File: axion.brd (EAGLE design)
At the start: 100 x 80.5 mm, 148 parts, among them IC1 3.3V, IC2 5V, Q2 12.288Mhz, U10 MIC2039, U11 WM8731, U2 Intel Edison, U4 FT232RLSSOP, U5 PCA9306D, U6 74HC4050, U7 TPA2005D1DGN, X2 ZX62R-AB-5P, X3 ST-005-G, X4 ZX62R-B-5P

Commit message: Anyway, wired everything
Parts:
- removed C14, C15: 0.1u, resistor:C1608
- removed U5: PCA9306D, NXP_By_element14_Batch_1:SOIC127P600X175-8N
- added Q1, Q3: 200mA/50V, SparkFun-DiscreteSemi:SOT23-3
- added R38: 4.7k, resistor:R0603
- C24: device resistor:C0805 -> resistor:C1608
- JP26: value HDC1000 module -> HDC1000
- R1, R10, R11, R12, R13, R14, R15, R16, R17, R18, R19, R2, R20, R21, R22, R23, R24, R3, R31, R32, R34, R37, R4, R5, R6, R7, R8, R9: device resistor:M1206 -> resistor:R0603
- R25: value 200k -> 4.7k; device resistor:0309V -> resistor:R0603
- R27, R35, R40, R41, R42, R43, R44: device resistor:R1206 -> resistor:R0603
- R30, R36: value 820 -> 4.7k; device resistor:M1206 -> resistor:R0603
- moved R36 99.8 mm to (70.3, 38.5), turned to 90 degrees
- moved R30 94.3 mm to (65.3, 42.6), turned to 270 degrees
- moved JP26 52.1 mm to (82.8, 52.3), turned to 180 degrees
- moved C19 42.4 mm to (75.7, 77.4), turned to 90 degrees
- moved X2 34.5 mm to (98.0, 60.9)
- moved C16 33.5 mm to (92.8, 65.8)
- moved X4 29.5 mm to (97.8, 71.1)
- moved C2 23.5 mm to (73.8, 61.9), turned to 180 degrees
- moved R33 22.1 mm to (50.5, 47.7), turned to 90 degrees
- moved C1 21.5 mm to (30.7, 40.6)
- moved U1 21.2 mm to (32.7, 33.7)
- moved R25 20.2 mm to (50.1, 43.6), turned to 270 degrees
- moved C7 18.8 mm to (73.0, 58.9)
- moved R32 17.5 mm to (51.9, 54.8), turned to 90 degrees
- moved U3 17.4 mm to (67.6, 29.3)
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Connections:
- removed net 1V8I2S_RTX: U8.7
- removed net 3V3SCK: U11.24
- removed net 5VCLK: U3.26
- removed net N$10: C14.1, R25.2, U5.7, U5.8
- net +1V8: now also Q1.1, Q3.1, R25.1, R30.1; no longer C15.2, R30.2, R36.2, U5.2
- net +3V3: now also R36.1, R38.1; no longer R25.1
- net 1V8I2S_RXD: now also U8.7
- net 1V8SCL: now also Q1.2, R25.2; no longer R30.1, U5.3
- net 1V8SDA: now also Q3.2, R30.2; no longer R36.1, U5.4
- net 3V3SCL: now also Q1.3, R38.2, U11.24, U3.26; no longer U5.6
- net 3V3SDA: now also Q3.3, R36.2; no longer U5.5
- net DGND: no longer C14.2, C15.1, U5.1
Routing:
- net DGND: track 561.0 -> 338.9 mm, vias 4 -> 19
- net GND: track 234.9 -> 71.2 mm, vias 3 -> 4
- net N$10: track 60.7 -> 0.00 mm
- net N$39: track 46.3 -> 105.5 mm
- net 3V3SCL: track 91.1 -> 124.9 mm, vias 1 -> 5
- net USB_ID: track 79.2 -> 46.0 mm, vias 0 -> 2
- net AGND: track 168.6 -> 200.2 mm, vias 1 -> 7
- net +1V8: track 155.4 -> 128.4 mm, vias 6 -> 8
- net 1V8PWMLED: track 18.2 -> 44.9 mm, vias 3 -> 1
- net USB_DP: track 74.4 -> 51.2 mm
- net 1P0: track 31.8 -> 11.9 mm
- net 1P1: track 28.6 -> 9.12 mm
- net N$8: track 0.00 -> 19.4 mm
- net N$49: track 0.00 -> 19.4 mm
- net 1P10: track 14.5 -> 33.4 mm, vias 0 -> 2
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
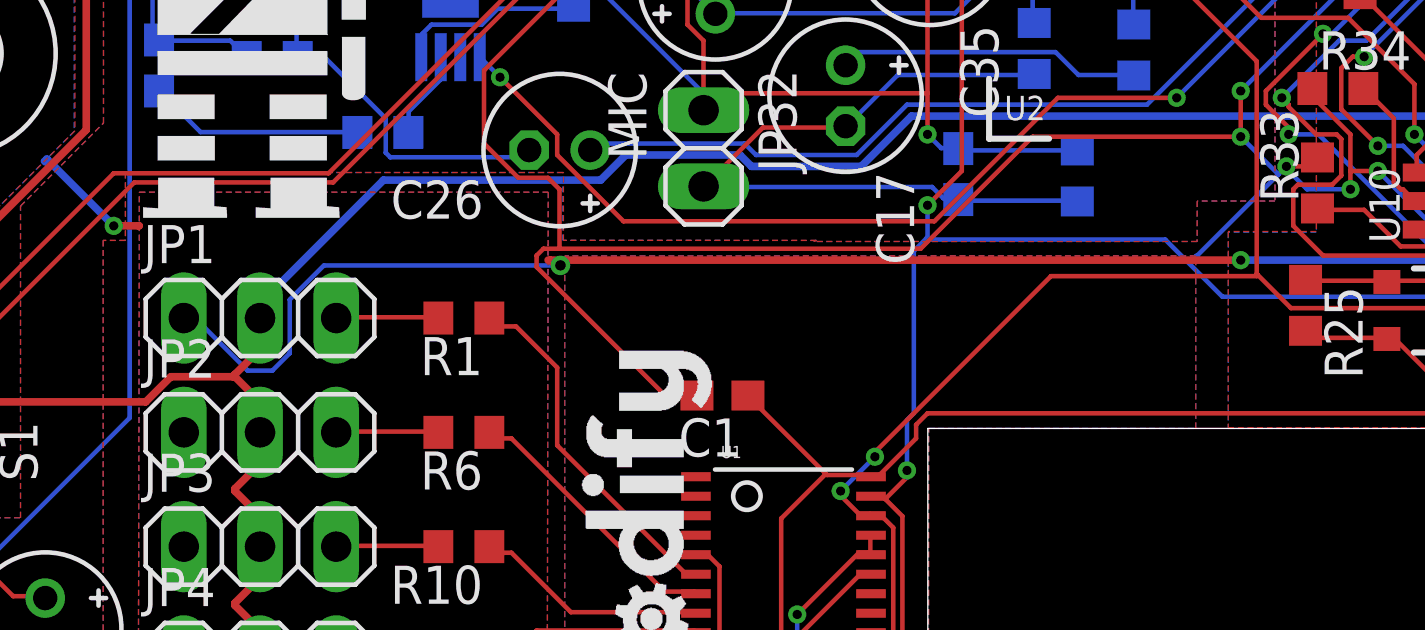
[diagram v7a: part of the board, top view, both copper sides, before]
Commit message: Fix all 'Width' DRC errors
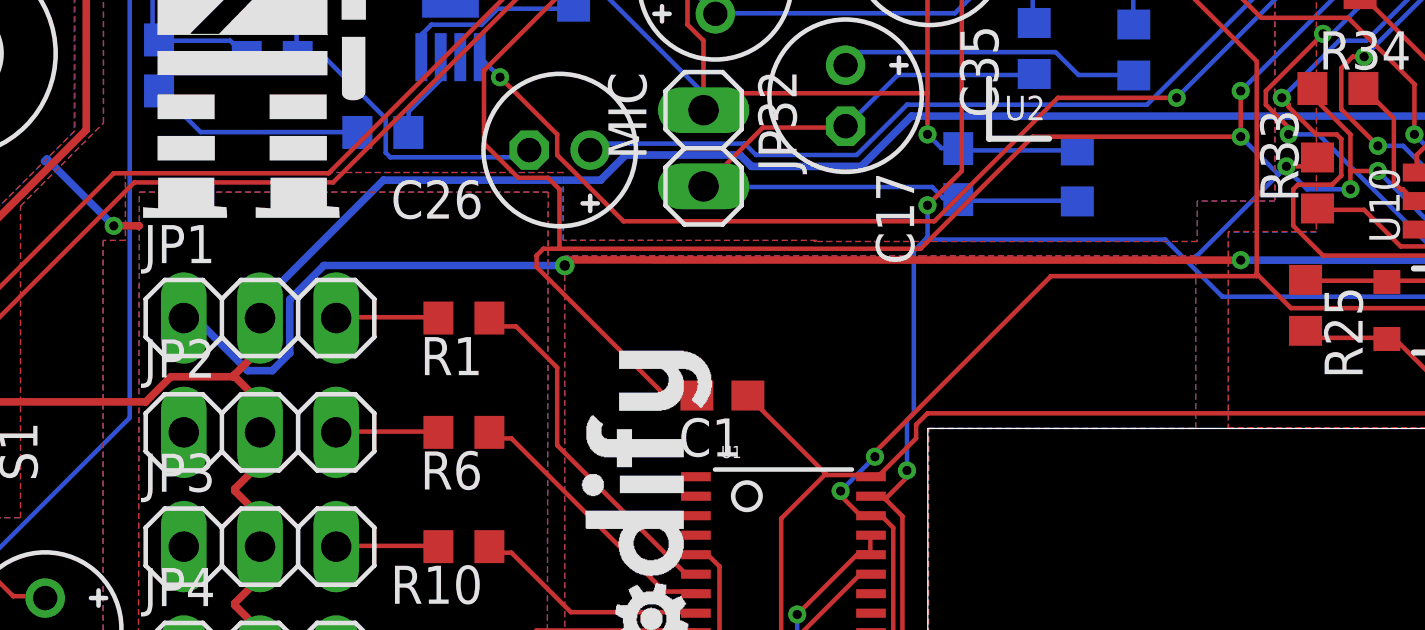
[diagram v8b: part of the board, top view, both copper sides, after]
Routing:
- net GND: track 71.2 -> 70.5 mm
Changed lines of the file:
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@@
 <contactref element="C3" pad="2"/>
 <contactref element="I2" pad="P$3"/>
-<polygon width="0.1524" layer="1" orphans="yes">
+<polygon width="0.254" layer="1" orphans="yes">
 <vertex x="0" y="37.12565625"/>
 <vertex x="0" y="80.55"/>
@@
 <vertex x="0.073153125" y="37.198809375"/>
 </polygon>
-<polygon width="0.1524" layer="16" orphans="yes">
+<polygon width="0.254" layer="16" orphans="yes">
 <vertex x="0" y="80.55"/>
 <vertex x="34.72205625" y="80.55"/>
@@
 <vertex x="0.045721875" y="37.17265"/>
 </polygon>
-<polygon width="0.1524" layer="16" orphans="yes" thermals="no">
+<polygon width="0.254" layer="16" orphans="yes" thermals="no">
 <vertex x="11.12799375" y="0"/>
 <vertex x="11.21799375" y="47.377665625"/>
@@
 <vertex x="24.75661875" y="0"/>
 </polygon>
-<polygon width="0.1524" layer="1" orphans="yes" thermals="no">
+<polygon width="0.254" layer="1" orphans="yes" thermals="no">
 <vertex x="11.12799375" y="0"/>
 <vertex x="11.21799375" y="47.377665625"/>
@@
 <vertex x="24.75661875" y="0"/>
 </polygon>
-<polygon width="0.1524" layer="1" orphans="yes" thermals="no">
+<polygon width="0.254" layer="1" orphans="yes" thermals="no">
 <vertex x="88.988390625" y="0"/>
 <vertex x="88.988390625" y="48.0771125"/>
@@
 <wire x1="8.1534" y1="48.4632" x2="8.131175" y2="48.485428125" width="0.254" layer="16"/>
 <wire x1="8.0772" y1="48.387" x2="8.054975" y2="48.409228125" width="0.254" layer="16"/>
-<wire x1="47.9298" y1="45.1104" x2="24.9174" y2="45.1104" width="0.254" layer="1"/>
+<wire x1="47.9298" y1="45.1104" x2="25.4094" y2="45.1174" width="0.254" layer="1"/>
 <wire x1="54.1782" y1="45.1104" x2="47.9298" y2="45.1104" width="0.254" layer="16"/>
 <wire x1="54.3306" y1="44.958" x2="54.1782" y2="45.1104" width="0.254" layer="16"/>
@@
 <wire x1="75.2094" y1="45.1866" x2="58.8264" y2="45.1866" width="0.254" layer="16"/>
 <wire x1="75.623928125" y1="45.1866" x2="75.2094" y2="45.1866" width="0.254" layer="1"/>
-<wire x1="24.9174" y1="45.1104" x2="24.8423125" y2="45.110834375" width="0.254" layer="1"/>
 <via x="10.3632" y="46.2534" extent="1-16" drill="0.3048"/>
 <via x="47.9298" y="45.1104" extent="1-16" drill="0.3048"/>
 <via x="75.2094" y="45.1866" extent="1-16" drill="0.3048"/>
-<wire x1="24.8423125" y1="45.110834375" x2="25.017746875" y2="44.9354" width="0.1524" layer="1"/>
-<wire x1="25.017746875" y1="44.9354" x2="25.25445" y2="44.9354" width="0.1524" layer="1"/>
-<via x="25.25445" y="44.9354" extent="1-16" drill="0.35"/>
-<wire x1="16.2306" y1="42.007675" x2="15.650325" y2="41.4274" width="0.1524" layer="16"/>
-<wire x1="15.650325" y1="41.4274" x2="14.829675" y2="41.4274" width="0.1524" layer="16"/>
-<wire x1="13.077075" y1="43.18" x2="12.7" y2="43.18" width="0.1524" layer="16"/>
-<wire x1="14.829675" y1="41.4274" x2="13.077075" y2="43.18" width="0.1524" layer="16"/>
-<wire x1="25.25445" y1="44.9354" x2="25.25165" y2="44.9326" width="0.1524" layer="16"/>
-<wire x1="25.25165" y1="44.9326" x2="17.369675" y2="44.9326" width="0.1524" layer="16"/>
-<wire x1="17.369675" y1="44.9326" x2="16.2306" y2="43.793525" width="0.1524" layer="16"/>
-<wire x1="16.2306" y1="43.793525" x2="16.2306" y2="42.007675" width="0.1524" layer="16"/>
+<via x="25.39845" y="44.9314" extent="1-16" drill="0.35"/>
+<wire x1="16.2306" y1="42.007675" x2="15.650325" y2="41.4274" width="0.254" layer="16"/>
+<wire x1="15.650325" y1="41.4274" x2="14.829675" y2="41.4274" width="0.254" layer="16"/>
+<wire x1="13.077075" y1="43.18" x2="12.7" y2="43.18" width="0.254" layer="16"/>
+<wire x1="14.829675" y1="41.4274" x2="13.077075" y2="43.18" width="0.254" layer="16"/>
+<wire x1="25.39845" y1="44.9314" x2="25.25165" y2="44.9326" width="0.254" layer="16"/>
+<wire x1="25.25165" y1="44.9326" x2="17.369675" y2="44.9326" width="0.254" layer="16"/>
+<wire x1="17.369675" y1="44.9326" x2="16.2306" y2="43.793525" width="0.254" layer="16"/>
+<wire x1="16.2306" y1="43.793525" x2="16.2306" y2="42.007675" width="0.254" layer="16"/>
+<wire x1="25.4094" y1="45.1174" x2="25.40145" y2="45.10945" width="0.254" layer="1"/>
+<wire x1="25.40145" y1="45.10945" x2="25.39845" y2="44.9314" width="0.254" layer="1"/>
 </signal>
 <signal name="DGND" class="2">
@@
 </signal>
 <signal name="N$36">
-<polygon width="0.1524" layer="16" orphans="yes" thermals="no">
+<polygon width="0.254" layer="16" orphans="yes" thermals="no">
 <vertex x="88.988390625" y="0"/>
 <vertex x="88.988390625" y="48.0771125"/>
